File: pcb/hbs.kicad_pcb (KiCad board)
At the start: 2 copper layers, 45.7 x 48.3 mm, 11 parts, among them Q1 BC337, U1 RobotDynProMini

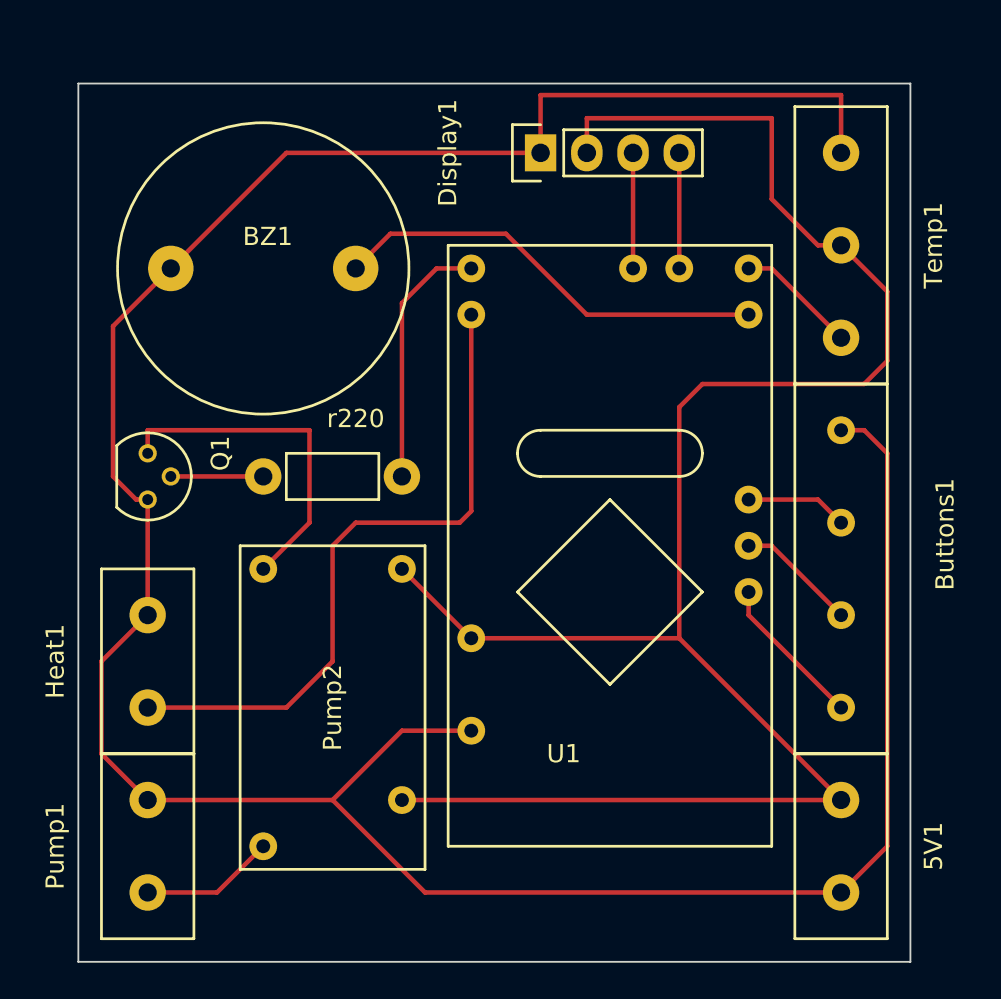
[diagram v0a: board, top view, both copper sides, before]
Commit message: Change relay footprint and cosmetic changes to schematic
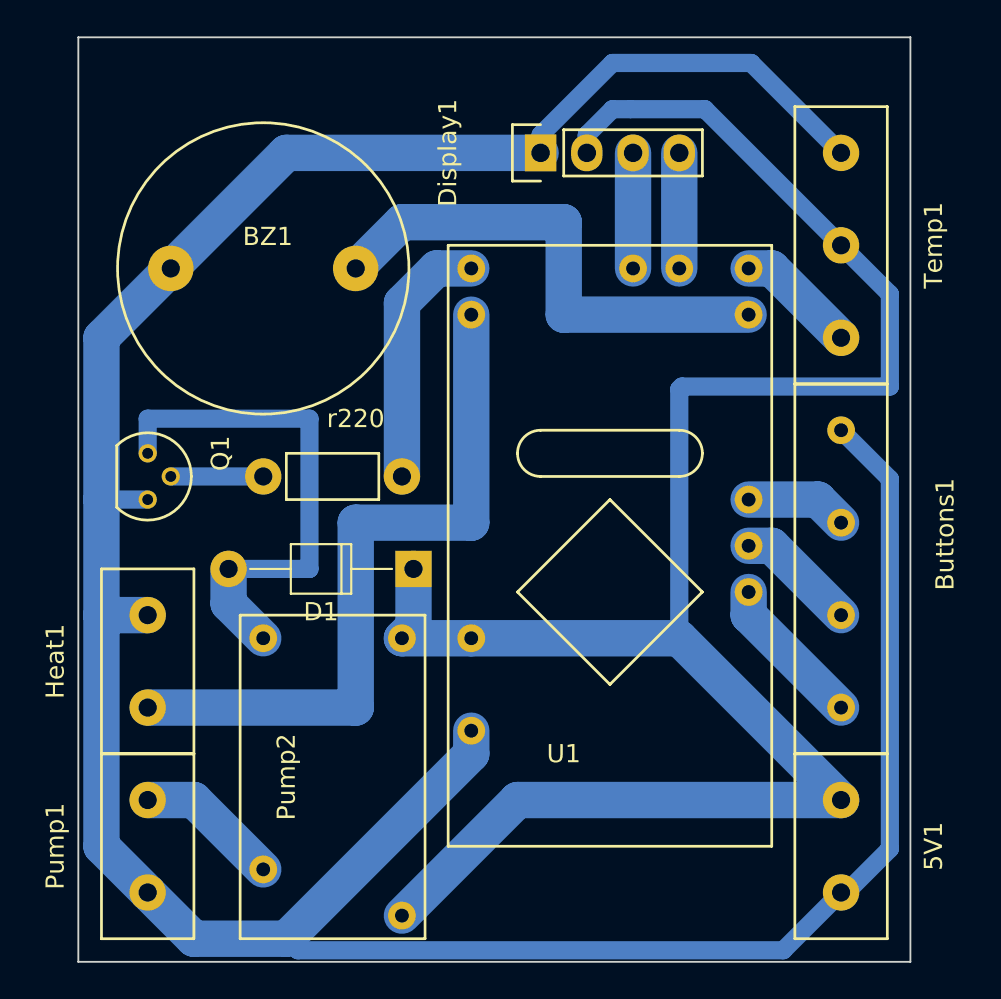
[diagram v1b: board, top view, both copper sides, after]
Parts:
- added D1: 1N4148, Diodes_THT:D_T-1_P10.16mm_Horizontal, F.Cu at (174.6, 128.3)
- moved Pump2 3.81 mm to (166.4, 132.1)
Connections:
- Pump1 pad 1: Net-(Pump1-Pad1) -> GND
- Pump1 pad 2: GND -> Net-(Pump1-Pad2)
- Pump2 pad 14: Net-(Pump1-Pad1) -> Net-(Pump1-Pad2)
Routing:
- net GND: track 157.3 -> 170.3 mm
- net Net-(D1-Pad2): track 18.8 -> 28.1 mm
- net Net-(Pump1-Pad2): track 0.00 -> 7.93 mm
- net Net-(Pump1-Pad1): track 7.40 -> 0.00 mm
- net VCC: track 107.5 -> 112.5 mm
- net Net-(BZ1-Pad2): track 24.2 -> 27.7 mm
- net Net-(Heat1-Pad2): track 36.8 -> 39.4 mm
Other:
- board size 45.7 x 48.3 mm -> 45.7 x 50.8 mm
